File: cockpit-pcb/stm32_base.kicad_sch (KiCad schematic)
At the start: 41 parts, among them J1 Network Connector, J2 B2B STLink connector, SW1 SW_Push, U1 LD39050PU33R, U2 STM32G474RBT6, U3 SN65HVD230, Y1 8MHz

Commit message: Board routing
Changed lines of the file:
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@@
 	)
 	(hierarchical_label "PB13"
-		(shape output)
+		(shape input)
 		(at 101.6 171.45 0)
 		(effects
@@
 	)
 	(hierarchical_label "PA8"
-		(shape input)
+		(shape output)
 		(at 101.6 115.57 0)
 		(effects
@@
 	)
 	(hierarchical_label "PB11"
-		(shape output)
+		(shape input)
 		(at 101.6 166.37 0)
 		(effects
@@
 	)
 	(hierarchical_label "PA7"
-		(shape input)
+		(shape output)
 		(at 101.6 113.03 0)
 		(effects
@@
 	)
 	(hierarchical_label "PB12"
-		(shape output)
+		(shape input)
 		(at 101.6 168.91 0)
 		(effects
@@
 	)
 	(hierarchical_label "PA6"
-		(shape input)
+		(shape output)
 		(at 101.6 110.49 0)
 		(effects

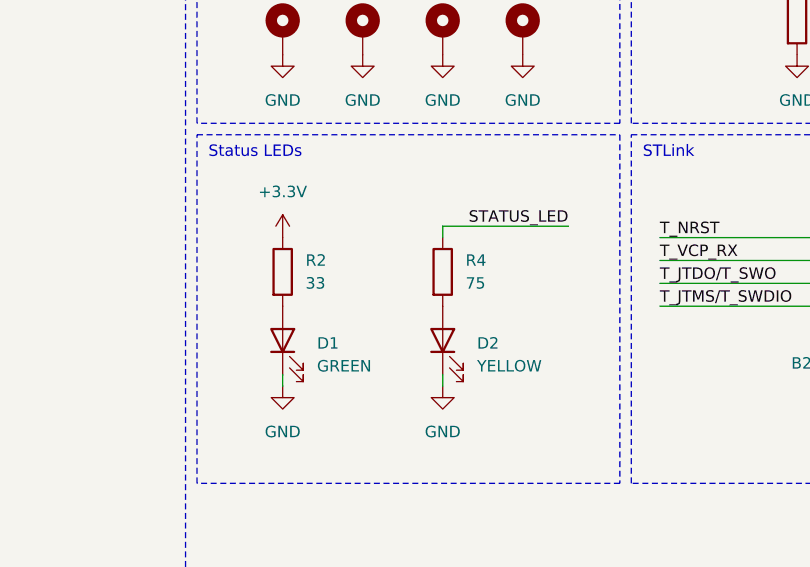
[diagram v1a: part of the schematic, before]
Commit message: Increase LED resistors
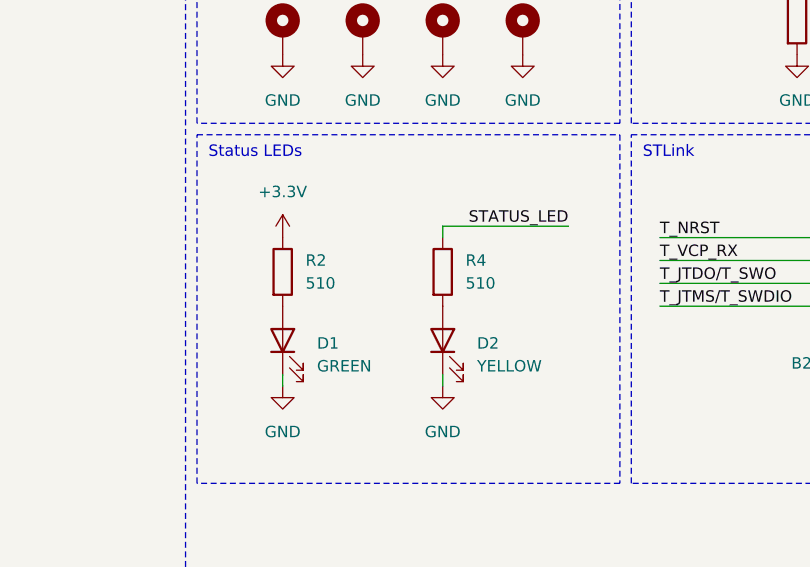
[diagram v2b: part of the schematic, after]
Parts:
- R2: value 33 -> 510; JLCPCB C23140 -> C23193
- R4: value 75 -> 510; JLCPCB C4275 -> C23193
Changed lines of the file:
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@@
 			)
 		)
-		(property "Value" "33"
+		(property "Value" "510"
 			(at 189.23 134.6199 0)
 			(effects
@@
 			)
 		)
-		(property "JLCPCB" "C23140"
+		(property "JLCPCB" "C23193"
 			(at 186.69 133.35 0)
 			(effects
@@
 			)
 		)
-		(property "Value" "75"
+		(property "Value" "510"
 			(at 207.01 134.6199 0)
 			(effects
@@
 			)
 		)
-		(property "JLCPCB" "C4275"
+		(property "JLCPCB" "C23193"
 			(at 204.47 133.35 0)
 			(effects

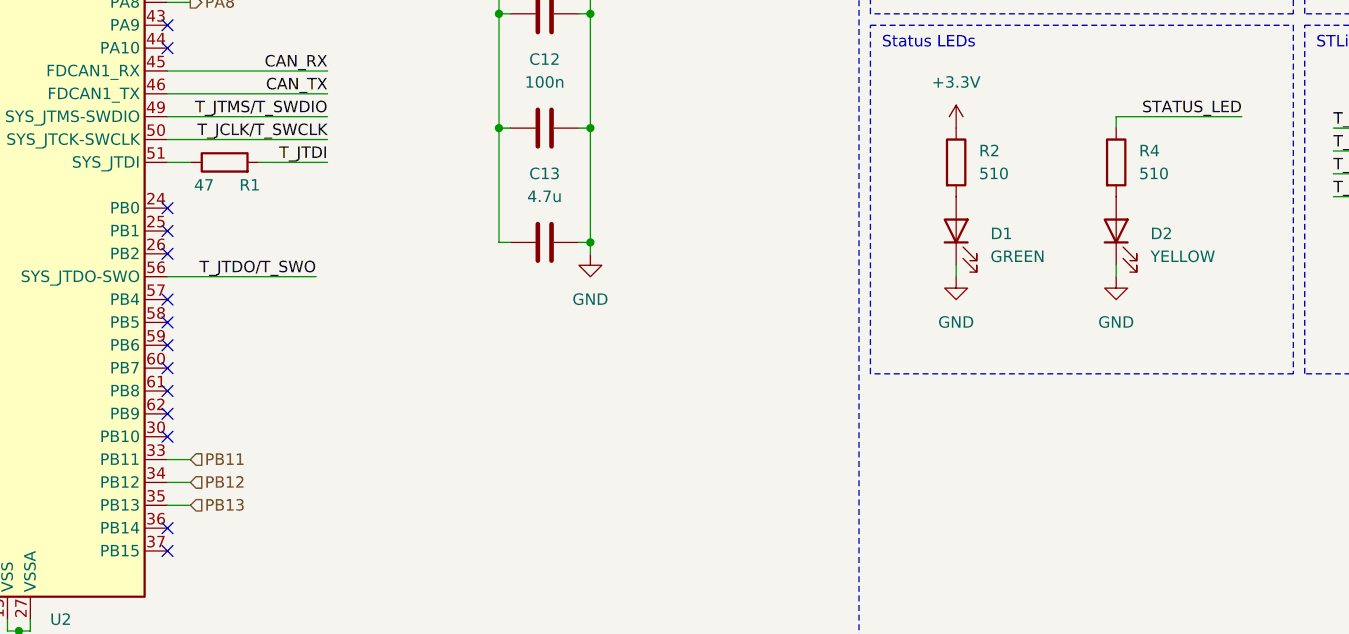
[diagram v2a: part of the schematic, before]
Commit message: cockpit: add PMBs
- Added 10k pull-down on boot0 (PB8) pin
- Increased SMD LED series resistor from 510 ohm to 1.1 kOhm
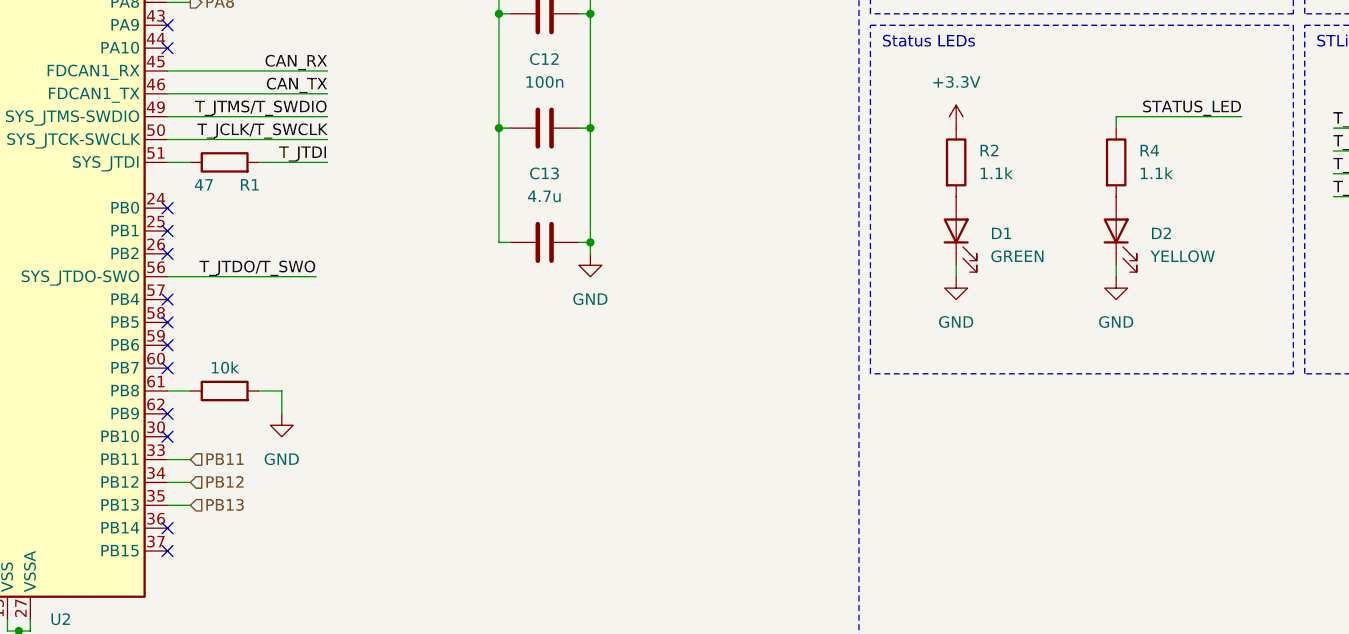
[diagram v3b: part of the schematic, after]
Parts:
- added PMB_R1: 10k, symbol Device:R
- R2, R4: value 510 -> 1.1k
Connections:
- net GND: now also PMB_R1.2
- net at U2.61 (PB8): now also PMB_R1.1
- no-connect marks 37 -> 36
